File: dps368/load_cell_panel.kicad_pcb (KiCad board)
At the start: 2 copper layers, 50 x 46 mm, 96 parts, among them J1 Conn_01x05_Female, U1 DPS368XTSA1

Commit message: goddamn it
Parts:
- removed the C1 at (164.3, 101.3)
- removed the C1 at (153.3, 81.3)
- removed the C1 at (142.3, 81.3)
- removed the C1 at (131.3, 81.3)
- removed the C1 at (164.3, 71.3)
- removed the C1 at (153.3, 71.3)
- removed the C1 at (142.3, 71.3)
- removed the C1 at (153.3, 101.3)
- removed the C1 at (142.3, 101.3)
- removed the C1 at (131.3, 101.3)
- removed the C1 at (164.3, 91.3)
- removed the C1 at (153.3, 91.3)
- removed the C1 at (142.3, 91.3)
- removed the C1 at (131.3, 91.3)
- removed the C1 at (164.3, 81.3)
- removed the C2 at (164.3, 103.3)
- removed the C2 at (153.3, 83.3)
- removed the C2 at (142.3, 83.3)
- removed the C2 at (131.3, 83.3)
- removed the C2 at (164.3, 73.3)
- removed the C2 at (153.3, 73.3)
- removed the C2 at (142.3, 73.3)
- removed the C2 at (153.3, 103.3)
- removed the C2 at (142.3, 103.3)
- removed the C2 at (131.3, 103.3)
- removed the C2 at (164.3, 93.3)
- removed the C2 at (153.3, 93.3)
- removed the C2 at (142.3, 93.3)
- removed the C2 at (131.3, 93.3)
- removed the C2 at (164.3, 83.3)
- removed the J1 at (163.9, 105.1)
- removed the J1 at (152.9, 85.1)
- removed the J1 at (141.9, 85.1)
- removed the J1 at (130.9, 85.1)
- removed the J1 at (163.9, 75.1)
- removed the J1 at (152.9, 75.1)
- removed the J1 at (141.9, 75.1)
- removed the J1 at (152.9, 105.1)
- removed the J1 at (141.9, 105.1)
- removed the J1 at (130.9, 105.1)
- removed the J1 at (163.9, 95.1)
- removed the J1 at (152.9, 95.1)
- removed the J1 at (141.9, 95.1)
- removed the J1 at (130.9, 95.1)
- removed the J1 at (163.9, 85.1)
- removed the R1 at (168.3, 103.3)
- removed the R1 at (157.3, 83.3)
- removed the R1 at (146.3, 83.3)
- removed the R1 at (135.3, 83.3)
- removed the R1 at (168.3, 73.3)
- removed the R1 at (157.3, 73.3)
- removed the R1 at (146.3, 73.3)
- removed the R1 at (157.3, 103.3)
- removed the R1 at (146.3, 103.3)
- removed the R1 at (135.3, 103.3)
- removed the R1 at (168.3, 93.3)
- removed the R1 at (157.3, 93.3)
- removed the R1 at (146.3, 93.3)
- removed the R1 at (135.3, 93.3)
- removed the R1 at (168.3, 83.3)
- removed the R2 at (168.3, 101.3)
- removed the R2 at (157.3, 81.3)
- removed the R2 at (146.3, 81.3)
- removed the R2 at (135.3, 81.3)
- removed the R2 at (168.3, 71.3)
- removed the R2 at (157.3, 71.3)
- removed the R2 at (146.3, 71.3)
- removed the R2 at (157.3, 101.3)
- removed the R2 at (146.3, 101.3)
- removed the R2 at (135.3, 101.3)
- removed the R2 at (168.3, 91.3)
- removed the R2 at (157.3, 91.3)
- removed the R2 at (146.3, 91.3)
- removed the R2 at (135.3, 91.3)
- removed the R2 at (168.3, 81.3)
- removed the U1 at (166.3, 101.8)
- removed the U1 at (155.3, 81.8)
- removed the U1 at (144.3, 81.8)
- removed the U1 at (133.3, 81.8)
- removed the U1 at (166.3, 71.8)
- removed the U1 at (155.3, 71.8)
- removed the U1 at (144.3, 71.8)
- removed the U1 at (155.3, 101.8)
- removed the U1 at (144.3, 101.8)
- removed the U1 at (133.3, 101.8)
- removed the U1 at (166.3, 91.8)
- removed the U1 at (155.3, 91.8)
- removed the U1 at (144.3, 91.8)
- removed the U1 at (133.3, 91.8)
- removed the U1 at (166.3, 81.8)
- added C1: 100n, Capacitor_SMD:C_0402_1005Metric, F.Cu at (164.0, 100.8)
- added C1: 100n, Capacitor_SMD:C_0402_1005Metric, F.Cu at (153.0, 80.8)
- added C1: 100n, Capacitor_SMD:C_0402_1005Metric, F.Cu at (142.0, 80.8)
- added C1: 100n, Capacitor_SMD:C_0402_1005Metric, F.Cu at (131.0, 80.8)
- added C1: 100n, Capacitor_SMD:C_0402_1005Metric, F.Cu at (164.0, 70.8)
- added C1: 100n, Capacitor_SMD:C_0402_1005Metric, F.Cu at (153.0, 70.8)
- added C1: 100n, Capacitor_SMD:C_0402_1005Metric, F.Cu at (142.0, 70.8)
- added C1: 100n, Capacitor_SMD:C_0402_1005Metric, F.Cu at (153.0, 100.8)
- added C1: 100n, Capacitor_SMD:C_0402_1005Metric, F.Cu at (142.0, 100.8)
- added C1: 100n, Capacitor_SMD:C_0402_1005Metric, F.Cu at (131.0, 100.8)
- added C1: 100n, Capacitor_SMD:C_0402_1005Metric, F.Cu at (164.0, 90.8)
- added C1: 100n, Capacitor_SMD:C_0402_1005Metric, F.Cu at (153.0, 90.8)
- added C1: 100n, Capacitor_SMD:C_0402_1005Metric, F.Cu at (142.0, 90.8)
- added C1: 100n, Capacitor_SMD:C_0402_1005Metric, F.Cu at (131.0, 90.8)
- added C1: 100n, Capacitor_SMD:C_0402_1005Metric, F.Cu at (164.0, 80.8)
- added C2: 100n, Capacitor_SMD:C_0402_1005Metric, F.Cu at (164.0, 102.8)
- added C2: 100n, Capacitor_SMD:C_0402_1005Metric, F.Cu at (153.0, 82.8)
- added C2: 100n, Capacitor_SMD:C_0402_1005Metric, F.Cu at (142.0, 82.8)
- added C2: 100n, Capacitor_SMD:C_0402_1005Metric, F.Cu at (131.0, 82.8)
- added C2: 100n, Capacitor_SMD:C_0402_1005Metric, F.Cu at (164.0, 72.8)
- added C2: 100n, Capacitor_SMD:C_0402_1005Metric, F.Cu at (153.0, 72.8)
- added C2: 100n, Capacitor_SMD:C_0402_1005Metric, F.Cu at (142.0, 72.8)
- added C2: 100n, Capacitor_SMD:C_0402_1005Metric, F.Cu at (153.0, 102.8)
- added C2: 100n, Capacitor_SMD:C_0402_1005Metric, F.Cu at (142.0, 102.8)
- added C2: 100n, Capacitor_SMD:C_0402_1005Metric, F.Cu at (131.0, 102.8)
- added C2: 100n, Capacitor_SMD:C_0402_1005Metric, F.Cu at (164.0, 92.8)
- added C2: 100n, Capacitor_SMD:C_0402_1005Metric, F.Cu at (153.0, 92.8)
- added C2: 100n, Capacitor_SMD:C_0402_1005Metric, F.Cu at (142.0, 92.8)
- added C2: 100n, Capacitor_SMD:C_0402_1005Metric, F.Cu at (131.0, 92.8)
- added C2: 100n, Capacitor_SMD:C_0402_1005Metric, F.Cu at (164.0, 82.8)
- added J1: Conn_01x05_Female, Connector_PinHeader_1.27mm:PinHeader_1x05_P1.27mm_Vertical, F.Cu at (163.6, 104.6)
- added J1: Conn_01x05_Female, Connector_PinHeader_1.27mm:PinHeader_1x05_P1.27mm_Vertical, F.Cu at (152.6, 84.6)
- added J1: Conn_01x05_Female, Connector_PinHeader_1.27mm:PinHeader_1x05_P1.27mm_Vertical, F.Cu at (141.6, 84.6)
- added J1: Conn_01x05_Female, Connector_PinHeader_1.27mm:PinHeader_1x05_P1.27mm_Vertical, F.Cu at (130.6, 84.6)
- added J1: Conn_01x05_Female, Connector_PinHeader_1.27mm:PinHeader_1x05_P1.27mm_Vertical, F.Cu at (163.6, 74.6)
- added J1: Conn_01x05_Female, Connector_PinHeader_1.27mm:PinHeader_1x05_P1.27mm_Vertical, F.Cu at (152.6, 74.6)
- added J1: Conn_01x05_Female, Connector_PinHeader_1.27mm:PinHeader_1x05_P1.27mm_Vertical, F.Cu at (141.6, 74.6)
- added J1: Conn_01x05_Female, Connector_PinHeader_1.27mm:PinHeader_1x05_P1.27mm_Vertical, F.Cu at (152.6, 104.6)
- added J1: Conn_01x05_Female, Connector_PinHeader_1.27mm:PinHeader_1x05_P1.27mm_Vertical, F.Cu at (141.6, 104.6)
- added J1: Conn_01x05_Female, Connector_PinHeader_1.27mm:PinHeader_1x05_P1.27mm_Vertical, F.Cu at (130.6, 104.6)
- added J1: Conn_01x05_Female, Connector_PinHeader_1.27mm:PinHeader_1x05_P1.27mm_Vertical, F.Cu at (163.6, 94.6)
- added J1: Conn_01x05_Female, Connector_PinHeader_1.27mm:PinHeader_1x05_P1.27mm_Vertical, F.Cu at (152.6, 94.6)
- added J1: Conn_01x05_Female, Connector_PinHeader_1.27mm:PinHeader_1x05_P1.27mm_Vertical, F.Cu at (141.6, 94.6)
- added J1: Conn_01x05_Female, Connector_PinHeader_1.27mm:PinHeader_1x05_P1.27mm_Vertical, F.Cu at (130.6, 94.6)
- added J1: Conn_01x05_Female, Connector_PinHeader_1.27mm:PinHeader_1x05_P1.27mm_Vertical, F.Cu at (163.6, 84.6)
- added R1: 10k, Resistor_SMD:R_0402_1005Metric, F.Cu at (168.0, 102.8)
- added R1: 10k, Resistor_SMD:R_0402_1005Metric, F.Cu at (157.0, 82.8)
- added R1: 10k, Resistor_SMD:R_0402_1005Metric, F.Cu at (146.0, 82.8)
- added R1: 10k, Resistor_SMD:R_0402_1005Metric, F.Cu at (135.0, 82.8)
- added R1: 10k, Resistor_SMD:R_0402_1005Metric, F.Cu at (168.0, 72.8)
- added R1: 10k, Resistor_SMD:R_0402_1005Metric, F.Cu at (157.0, 72.8)
- added R1: 10k, Resistor_SMD:R_0402_1005Metric, F.Cu at (146.0, 72.8)
- added R1: 10k, Resistor_SMD:R_0402_1005Metric, F.Cu at (157.0, 102.8)
- added R1: 10k, Resistor_SMD:R_0402_1005Metric, F.Cu at (146.0, 102.8)
- added R1: 10k, Resistor_SMD:R_0402_1005Metric, F.Cu at (135.0, 102.8)
- added R1: 10k, Resistor_SMD:R_0402_1005Metric, F.Cu at (168.0, 92.8)
- added R1: 10k, Resistor_SMD:R_0402_1005Metric, F.Cu at (157.0, 92.8)
- added R1: 10k, Resistor_SMD:R_0402_1005Metric, F.Cu at (146.0, 92.8)
- added R1: 10k, Resistor_SMD:R_0402_1005Metric, F.Cu at (135.0, 92.8)
- added R1: 10k, Resistor_SMD:R_0402_1005Metric, F.Cu at (168.0, 82.8)
- added R2: 10k, Resistor_SMD:R_0402_1005Metric, F.Cu at (168.0, 100.8)
- added R2: 10k, Resistor_SMD:R_0402_1005Metric, F.Cu at (157.0, 80.8)
- added R2: 10k, Resistor_SMD:R_0402_1005Metric, F.Cu at (146.0, 80.8)
- added R2: 10k, Resistor_SMD:R_0402_1005Metric, F.Cu at (135.0, 80.8)
- added R2: 10k, Resistor_SMD:R_0402_1005Metric, F.Cu at (168.0, 70.8)
- added R2: 10k, Resistor_SMD:R_0402_1005Metric, F.Cu at (157.0, 70.8)
- added R2: 10k, Resistor_SMD:R_0402_1005Metric, F.Cu at (146.0, 70.8)
- added R2: 10k, Resistor_SMD:R_0402_1005Metric, F.Cu at (157.0, 100.8)
- added R2: 10k, Resistor_SMD:R_0402_1005Metric, F.Cu at (146.0, 100.8)
- added R2: 10k, Resistor_SMD:R_0402_1005Metric, F.Cu at (135.0, 100.8)
- added R2: 10k, Resistor_SMD:R_0402_1005Metric, F.Cu at (168.0, 90.8)
- added R2: 10k, Resistor_SMD:R_0402_1005Metric, F.Cu at (157.0, 90.8)
- added R2: 10k, Resistor_SMD:R_0402_1005Metric, F.Cu at (146.0, 90.8)
- added R2: 10k, Resistor_SMD:R_0402_1005Metric, F.Cu at (135.0, 90.8)
- added R2: 10k, Resistor_SMD:R_0402_1005Metric, F.Cu at (168.0, 80.8)
- added U1: DPS368XTSA1, custom_lib:XDCR_DPS368XTSA1, F.Cu at (166.0, 101.3)
- added U1: DPS368XTSA1, custom_lib:XDCR_DPS368XTSA1, F.Cu at (155.0, 81.3)
- added U1: DPS368XTSA1, custom_lib:XDCR_DPS368XTSA1, F.Cu at (144.0, 81.3)
- added U1: DPS368XTSA1, custom_lib:XDCR_DPS368XTSA1, F.Cu at (133.0, 81.3)
- added U1: DPS368XTSA1, custom_lib:XDCR_DPS368XTSA1, F.Cu at (166.0, 71.3)
- added U1: DPS368XTSA1, custom_lib:XDCR_DPS368XTSA1, F.Cu at (155.0, 71.3)
- added U1: DPS368XTSA1, custom_lib:XDCR_DPS368XTSA1, F.Cu at (144.0, 71.3)
- added U1: DPS368XTSA1, custom_lib:XDCR_DPS368XTSA1, F.Cu at (155.0, 101.3)
- added U1: DPS368XTSA1, custom_lib:XDCR_DPS368XTSA1, F.Cu at (144.0, 101.3)
- added U1: DPS368XTSA1, custom_lib:XDCR_DPS368XTSA1, F.Cu at (133.0, 101.3)
- added U1: DPS368XTSA1, custom_lib:XDCR_DPS368XTSA1, F.Cu at (166.0, 91.3)
- added U1: DPS368XTSA1, custom_lib:XDCR_DPS368XTSA1, F.Cu at (155.0, 91.3)
- added U1: DPS368XTSA1, custom_lib:XDCR_DPS368XTSA1, F.Cu at (144.0, 91.3)
- added U1: DPS368XTSA1, custom_lib:XDCR_DPS368XTSA1, F.Cu at (133.0, 91.3)
- added U1: DPS368XTSA1, custom_lib:XDCR_DPS368XTSA1, F.Cu at (166.0, 81.3)
- moved C1 0.58 mm to (131.0, 70.8)
- moved C2 0.58 mm to (131.0, 72.8)
- moved J1 0.58 mm to (130.6, 74.6)
- moved R1 0.58 mm to (135.0, 72.8)
- moved R2 0.58 mm to (135.0, 70.8)
- moved U1 0.58 mm to (133.0, 71.3)
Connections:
- C1 pad 1: +3V3 -> GND
- C1 pad 2: Net-(C1-Pad2) -> +3V3
- C2 pad 1: Net-(C2-Pad1) -> GND
- U1 pad 6: Net-(C2-Pad1) -> +3V3
- U1 pad 8: Net-(C1-Pad2) -> +3V3
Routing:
- net +3V3: track 172.3 -> 235.8 mm
- net GND: track 107.3 -> 153.3 mm
- net Net-(C2-Pad1): track 42.5 -> 0.00 mm
- net Net-(C1-Pad2): track 20.6 -> 0.00 mm
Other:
- outline, holes or cut-outs redrawn

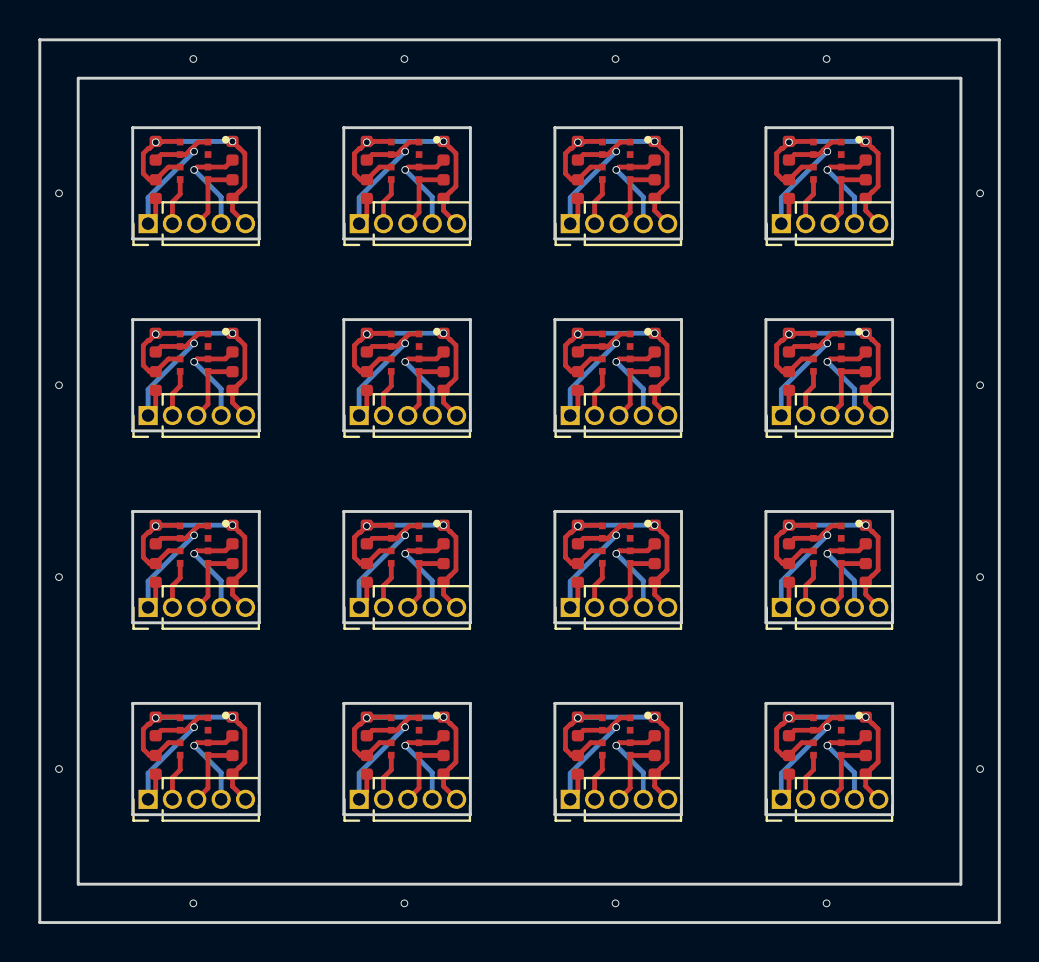
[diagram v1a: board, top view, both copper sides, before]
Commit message: 7mm diameter sensor
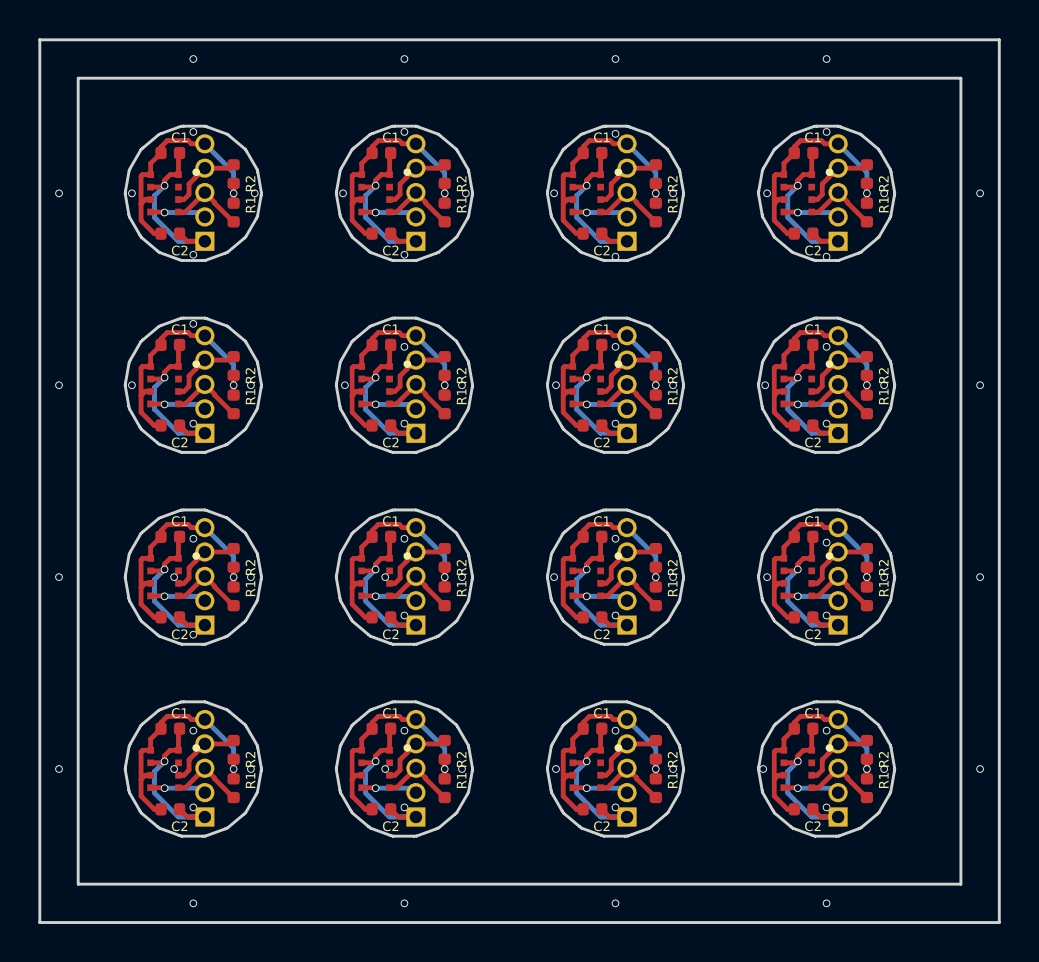
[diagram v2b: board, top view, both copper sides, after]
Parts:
- removed the C1 at (164.0, 100.8)
- removed the C1 at (153.0, 80.8)
- removed the C1 at (142.0, 80.8)
- removed the C1 at (131.0, 80.8)
- removed the C1 at (164.0, 70.8)
- removed the C1 at (153.0, 70.8)
- removed the C1 at (142.0, 70.8)
- removed the C1 at (153.0, 100.8)
- removed the C1 at (142.0, 100.8)
- removed the C1 at (131.0, 100.8)
- removed the C1 at (164.0, 90.8)
- removed the C1 at (153.0, 90.8)
- removed the C1 at (142.0, 90.8)
- removed the C1 at (131.0, 90.8)
- removed the C1 at (164.0, 80.8)
- removed the C2 at (164.0, 102.8)
- removed the C2 at (153.0, 82.8)
- removed the C2 at (142.0, 82.8)
- removed the C2 at (131.0, 82.8)
- removed the C2 at (164.0, 72.8)
- removed the C2 at (153.0, 72.8)
- removed the C2 at (142.0, 72.8)
- removed the C2 at (131.0, 72.8)
- removed the C2 at (153.0, 102.8)
- removed the C2 at (142.0, 102.8)
- removed the C2 at (131.0, 102.8)
- removed the C2 at (164.0, 92.8)
- removed the C2 at (153.0, 92.8)
- removed the C2 at (142.0, 92.8)
- removed the C2 at (131.0, 92.8)
- removed the C2 at (164.0, 82.8)
- removed the J1 at (163.6, 104.6)
- removed the J1 at (152.6, 84.6)
- removed the J1 at (141.6, 84.6)
- removed the J1 at (130.6, 84.6)
- removed the J1 at (163.6, 74.6)
- removed the J1 at (152.6, 74.6)
- removed the J1 at (141.6, 74.6)
- removed the J1 at (152.6, 104.6)
- removed the J1 at (141.6, 104.6)
- removed the J1 at (130.6, 104.6)
- removed the J1 at (163.6, 94.6)
- removed the J1 at (152.6, 94.6)
- removed the J1 at (141.6, 94.6)
- removed the J1 at (130.6, 94.6)
- removed the J1 at (163.6, 84.6)
- removed the R1 at (168.0, 102.8)
- removed the R1 at (157.0, 82.8)
- removed the R1 at (146.0, 82.8)
- removed the R1 at (135.0, 82.8)
- removed the R1 at (168.0, 72.8)
- removed the R1 at (157.0, 72.8)
- removed the R1 at (146.0, 72.8)
- removed the R1 at (157.0, 102.8)
- removed the R1 at (146.0, 102.8)
- removed the R1 at (135.0, 102.8)
- removed the R1 at (168.0, 92.8)
- removed the R1 at (157.0, 92.8)
- removed the R1 at (146.0, 92.8)
- removed the R1 at (135.0, 92.8)
- removed the R1 at (168.0, 82.8)
- removed the R2 at (168.0, 100.8)
- removed the R2 at (157.0, 80.8)
- removed the R2 at (146.0, 80.8)
- removed the R2 at (135.0, 80.8)
- removed the R2 at (168.0, 70.8)
- removed the R2 at (157.0, 70.8)
- removed the R2 at (146.0, 70.8)
- removed the R2 at (135.0, 70.8)
- removed the R2 at (157.0, 100.8)
- removed the R2 at (146.0, 100.8)
- removed the R2 at (135.0, 100.8)
- removed the R2 at (168.0, 90.8)
- removed the R2 at (157.0, 90.8)
- removed the R2 at (146.0, 90.8)
- removed the R2 at (135.0, 90.8)
- removed the R2 at (168.0, 80.8)
- removed the U1 at (166.0, 101.3)
- removed the U1 at (155.0, 81.3)
- removed the U1 at (144.0, 81.3)
- removed the U1 at (133.0, 81.3)
- removed the U1 at (166.0, 71.3)
- removed the U1 at (155.0, 71.3)
- removed the U1 at (144.0, 71.3)
- removed the U1 at (133.0, 71.3)
- removed the U1 at (155.0, 101.3)
- removed the U1 at (144.0, 101.3)
- removed the U1 at (133.0, 101.3)
- removed the U1 at (166.0, 91.3)
- removed the U1 at (155.0, 91.3)
- removed the U1 at (144.0, 91.3)
- removed the U1 at (133.0, 91.3)
- removed the U1 at (166.0, 81.3)
- added C1: 100n, Capacitor_SMD:C_0402_1005Metric, F.Cu at (164.8, 70.9)
- added C1: 100n, Capacitor_SMD:C_0402_1005Metric, F.Cu at (164.8, 80.9)
- added C1: 100n, Capacitor_SMD:C_0402_1005Metric, F.Cu at (153.8, 70.9)
- added C1: 100n, Capacitor_SMD:C_0402_1005Metric, F.Cu at (142.8, 100.9)
- added C1: 100n, Capacitor_SMD:C_0402_1005Metric, F.Cu at (131.8, 90.9)
- added C1: 100n, Capacitor_SMD:C_0402_1005Metric, F.Cu at (131.8, 100.9)
- added C1: 100n, Capacitor_SMD:C_0402_1005Metric, F.Cu at (131.8, 80.9)
- added C1: 100n, Capacitor_SMD:C_0402_1005Metric, F.Cu at (142.8, 90.9)
- added C1: 100n, Capacitor_SMD:C_0402_1005Metric, F.Cu at (153.8, 100.9)
- added C1: 100n, Capacitor_SMD:C_0402_1005Metric, F.Cu at (153.8, 90.9)
- added C1: 100n, Capacitor_SMD:C_0402_1005Metric, F.Cu at (164.8, 100.9)
- added C1: 100n, Capacitor_SMD:C_0402_1005Metric, F.Cu at (153.8, 80.9)
- added C1: 100n, Capacitor_SMD:C_0402_1005Metric, F.Cu at (164.8, 90.9)
- added C1: 100n, Capacitor_SMD:C_0402_1005Metric, F.Cu at (142.8, 70.9)
- added C1: 100n, Capacitor_SMD:C_0402_1005Metric, F.Cu at (142.8, 80.9)
- added C2: 100n, Capacitor_SMD:C_0402_1005Metric, F.Cu at (164.8, 95.1)
- added C2: 100n, Capacitor_SMD:C_0402_1005Metric, F.Cu at (153.8, 75.1)
- added C2: 100n, Capacitor_SMD:C_0402_1005Metric, F.Cu at (164.8, 105.1)
- added C2: 100n, Capacitor_SMD:C_0402_1005Metric, F.Cu at (164.8, 85.1)
- added C2: 100n, Capacitor_SMD:C_0402_1005Metric, F.Cu at (131.8, 105.1)
- added C2: 100n, Capacitor_SMD:C_0402_1005Metric, F.Cu at (131.8, 85.1)
- added C2: 100n, Capacitor_SMD:C_0402_1005Metric, F.Cu at (131.8, 95.1)
- added C2: 100n, Capacitor_SMD:C_0402_1005Metric, F.Cu at (131.8, 75.1)
- added C2: 100n, Capacitor_SMD:C_0402_1005Metric, F.Cu at (153.8, 95.1)
- added C2: 100n, Capacitor_SMD:C_0402_1005Metric, F.Cu at (142.8, 95.1)
- added C2: 100n, Capacitor_SMD:C_0402_1005Metric, F.Cu at (153.8, 105.1)
- added C2: 100n, Capacitor_SMD:C_0402_1005Metric, F.Cu at (142.8, 105.1)
- added C2: 100n, Capacitor_SMD:C_0402_1005Metric, F.Cu at (142.8, 75.1)
- added C2: 100n, Capacitor_SMD:C_0402_1005Metric, F.Cu at (153.8, 85.1)
- added C2: 100n, Capacitor_SMD:C_0402_1005Metric, F.Cu at (164.8, 75.1)
- added C2: 100n, Capacitor_SMD:C_0402_1005Metric, F.Cu at (142.8, 85.1)
- added J1: Conn_01x05_Female, Connector_PinHeader_1.27mm:PinHeader_1x05_P1.27mm_Vertical, B.Cu at (166.6, 95.5)
- added J1: Conn_01x05_Female, Connector_PinHeader_1.27mm:PinHeader_1x05_P1.27mm_Vertical, B.Cu at (155.6, 75.5)
- added J1: Conn_01x05_Female, Connector_PinHeader_1.27mm:PinHeader_1x05_P1.27mm_Vertical, B.Cu at (144.6, 75.5)
- added J1: Conn_01x05_Female, Connector_PinHeader_1.27mm:PinHeader_1x05_P1.27mm_Vertical, B.Cu at (166.6, 105.5)
- added J1: Conn_01x05_Female, Connector_PinHeader_1.27mm:PinHeader_1x05_P1.27mm_Vertical, B.Cu at (133.6, 105.5)
- added J1: Conn_01x05_Female, Connector_PinHeader_1.27mm:PinHeader_1x05_P1.27mm_Vertical, B.Cu at (133.6, 95.5)
- added J1: Conn_01x05_Female, Connector_PinHeader_1.27mm:PinHeader_1x05_P1.27mm_Vertical, B.Cu at (133.6, 85.5)
- added J1: Conn_01x05_Female, Connector_PinHeader_1.27mm:PinHeader_1x05_P1.27mm_Vertical, B.Cu at (155.6, 105.5)
- added J1: Conn_01x05_Female, Connector_PinHeader_1.27mm:PinHeader_1x05_P1.27mm_Vertical, B.Cu at (144.6, 105.5)
- added J1: Conn_01x05_Female, Connector_PinHeader_1.27mm:PinHeader_1x05_P1.27mm_Vertical, B.Cu at (155.6, 95.5)
- added J1: Conn_01x05_Female, Connector_PinHeader_1.27mm:PinHeader_1x05_P1.27mm_Vertical, B.Cu at (144.6, 95.5)
- added J1: Conn_01x05_Female, Connector_PinHeader_1.27mm:PinHeader_1x05_P1.27mm_Vertical, B.Cu at (166.6, 85.5)
- added J1: Conn_01x05_Female, Connector_PinHeader_1.27mm:PinHeader_1x05_P1.27mm_Vertical, B.Cu at (155.6, 85.5)
- added J1: Conn_01x05_Female, Connector_PinHeader_1.27mm:PinHeader_1x05_P1.27mm_Vertical, B.Cu at (144.6, 85.5)
- added J1: Conn_01x05_Female, Connector_PinHeader_1.27mm:PinHeader_1x05_P1.27mm_Vertical, B.Cu at (166.6, 75.5)
- added R1: 10k, Resistor_SMD:R_0402_1005Metric, F.Cu at (168.1, 74.0)
- added R1: 10k, Resistor_SMD:R_0402_1005Metric, F.Cu at (157.1, 84.0)
- added R1: 10k, Resistor_SMD:R_0402_1005Metric, F.Cu at (157.1, 74.0)
- added R1: 10k, Resistor_SMD:R_0402_1005Metric, F.Cu at (168.1, 84.0)
- added R1: 10k, Resistor_SMD:R_0402_1005Metric, F.Cu at (135.1, 104.0)
- added R1: 10k, Resistor_SMD:R_0402_1005Metric, F.Cu at (135.1, 84.0)
- added R1: 10k, Resistor_SMD:R_0402_1005Metric, F.Cu at (135.1, 94.0)
- added R1: 10k, Resistor_SMD:R_0402_1005Metric, F.Cu at (146.1, 94.0)
- added R1: 10k, Resistor_SMD:R_0402_1005Metric, F.Cu at (157.1, 94.0)
- added R1: 10k, Resistor_SMD:R_0402_1005Metric, F.Cu at (168.1, 94.0)
- added R1: 10k, Resistor_SMD:R_0402_1005Metric, F.Cu at (146.1, 84.0)
- added R1: 10k, Resistor_SMD:R_0402_1005Metric, F.Cu at (146.1, 74.0)
- added R1: 10k, Resistor_SMD:R_0402_1005Metric, F.Cu at (146.1, 104.0)
- added R1: 10k, Resistor_SMD:R_0402_1005Metric, F.Cu at (157.1, 104.0)
- added R1: 10k, Resistor_SMD:R_0402_1005Metric, F.Cu at (168.1, 104.0)
- added R2: 10k, Resistor_SMD:R_0402_1005Metric, F.Cu at (168.1, 92.0)
- added R2: 10k, Resistor_SMD:R_0402_1005Metric, F.Cu at (168.1, 102.0)
- added R2: 10k, Resistor_SMD:R_0402_1005Metric, F.Cu at (157.1, 72.0)
- added R2: 10k, Resistor_SMD:R_0402_1005Metric, F.Cu at (146.1, 72.0)
- added R2: 10k, Resistor_SMD:R_0402_1005Metric, F.Cu at (135.1, 82.0)
- added R2: 10k, Resistor_SMD:R_0402_1005Metric, F.Cu at (135.1, 102.0)
- added R2: 10k, Resistor_SMD:R_0402_1005Metric, F.Cu at (135.1, 92.0)
- added R2: 10k, Resistor_SMD:R_0402_1005Metric, F.Cu at (135.1, 72.0)
- added R2: 10k, Resistor_SMD:R_0402_1005Metric, F.Cu at (157.1, 92.0)
- added R2: 10k, Resistor_SMD:R_0402_1005Metric, F.Cu at (146.1, 92.0)
- added R2: 10k, Resistor_SMD:R_0402_1005Metric, F.Cu at (168.1, 72.0)
- added R2: 10k, Resistor_SMD:R_0402_1005Metric, F.Cu at (157.1, 102.0)
- added R2: 10k, Resistor_SMD:R_0402_1005Metric, F.Cu at (146.1, 102.0)
- added R2: 10k, Resistor_SMD:R_0402_1005Metric, F.Cu at (146.1, 82.0)
- added R2: 10k, Resistor_SMD:R_0402_1005Metric, F.Cu at (168.1, 82.0)
- added R2: 10k, Resistor_SMD:R_0402_1005Metric, F.Cu at (157.1, 82.0)
- added U1: DPS368XTSA1, custom_lib:XDCR_DPS368XTSA1, F.Cu at (164.5, 93.0)
- added U1: DPS368XTSA1, custom_lib:XDCR_DPS368XTSA1, F.Cu at (153.5, 103.0)
- added U1: DPS368XTSA1, custom_lib:XDCR_DPS368XTSA1, F.Cu at (153.5, 93.0)
- added U1: DPS368XTSA1, custom_lib:XDCR_DPS368XTSA1, F.Cu at (164.5, 83.0)
- added U1: DPS368XTSA1, custom_lib:XDCR_DPS368XTSA1, F.Cu at (131.5, 93.0)
- added U1: DPS368XTSA1, custom_lib:XDCR_DPS368XTSA1, F.Cu at (131.5, 103.0)
- added U1: DPS368XTSA1, custom_lib:XDCR_DPS368XTSA1, F.Cu at (131.5, 83.0)
- added U1: DPS368XTSA1, custom_lib:XDCR_DPS368XTSA1, F.Cu at (131.5, 73.0)
- added U1: DPS368XTSA1, custom_lib:XDCR_DPS368XTSA1, F.Cu at (142.5, 83.0)
- added U1: DPS368XTSA1, custom_lib:XDCR_DPS368XTSA1, F.Cu at (164.5, 103.0)
- added U1: DPS368XTSA1, custom_lib:XDCR_DPS368XTSA1, F.Cu at (164.5, 73.0)
- added U1: DPS368XTSA1, custom_lib:XDCR_DPS368XTSA1, F.Cu at (142.5, 103.0)
- added U1: DPS368XTSA1, custom_lib:XDCR_DPS368XTSA1, F.Cu at (142.5, 93.0)
- added U1: DPS368XTSA1, custom_lib:XDCR_DPS368XTSA1, F.Cu at (153.5, 73.0)
- added U1: DPS368XTSA1, custom_lib:XDCR_DPS368XTSA1, F.Cu at (153.5, 83.0)
- added U1: DPS368XTSA1, custom_lib:XDCR_DPS368XTSA1, F.Cu at (142.5, 73.0)
- J1: moved to B.Cu
- moved J1 3.10 mm to (133.6, 75.5), turned to 0 degrees
- moved R1 1.22 mm to (135.1, 74.0), turned to 270 degrees
- moved C1 0.77 mm to (131.8, 70.9), turned to 180 degrees
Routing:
- net /sdi: track 89.6 -> 63.1 mm, vias 16 -> 0
- net +3V3: track 235.8 -> 210.3 mm, vias 32 -> 16
- net /sdo: track 39.5 -> 46.9 mm, vias 0 -> 16
- net /sck: track 61.2 -> 63.2 mm
- net GND: track 153.3 -> 152.4 mm
- net (no net): vias 16 -> 80
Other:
- outline, holes or cut-outs redrawn
